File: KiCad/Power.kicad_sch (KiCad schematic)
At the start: 33 parts, among them J11 ATX_POWER_20, J12 Front Panel, Q3 2N3904, SW1 POWER, SW2 RESET, U106 LM7905_TO220, U130 74LS07, U401 74F32, U603 74HCT74, U604 74HCT14, U810 74F08, X1 14.31818MHz, X2 33.333MHz

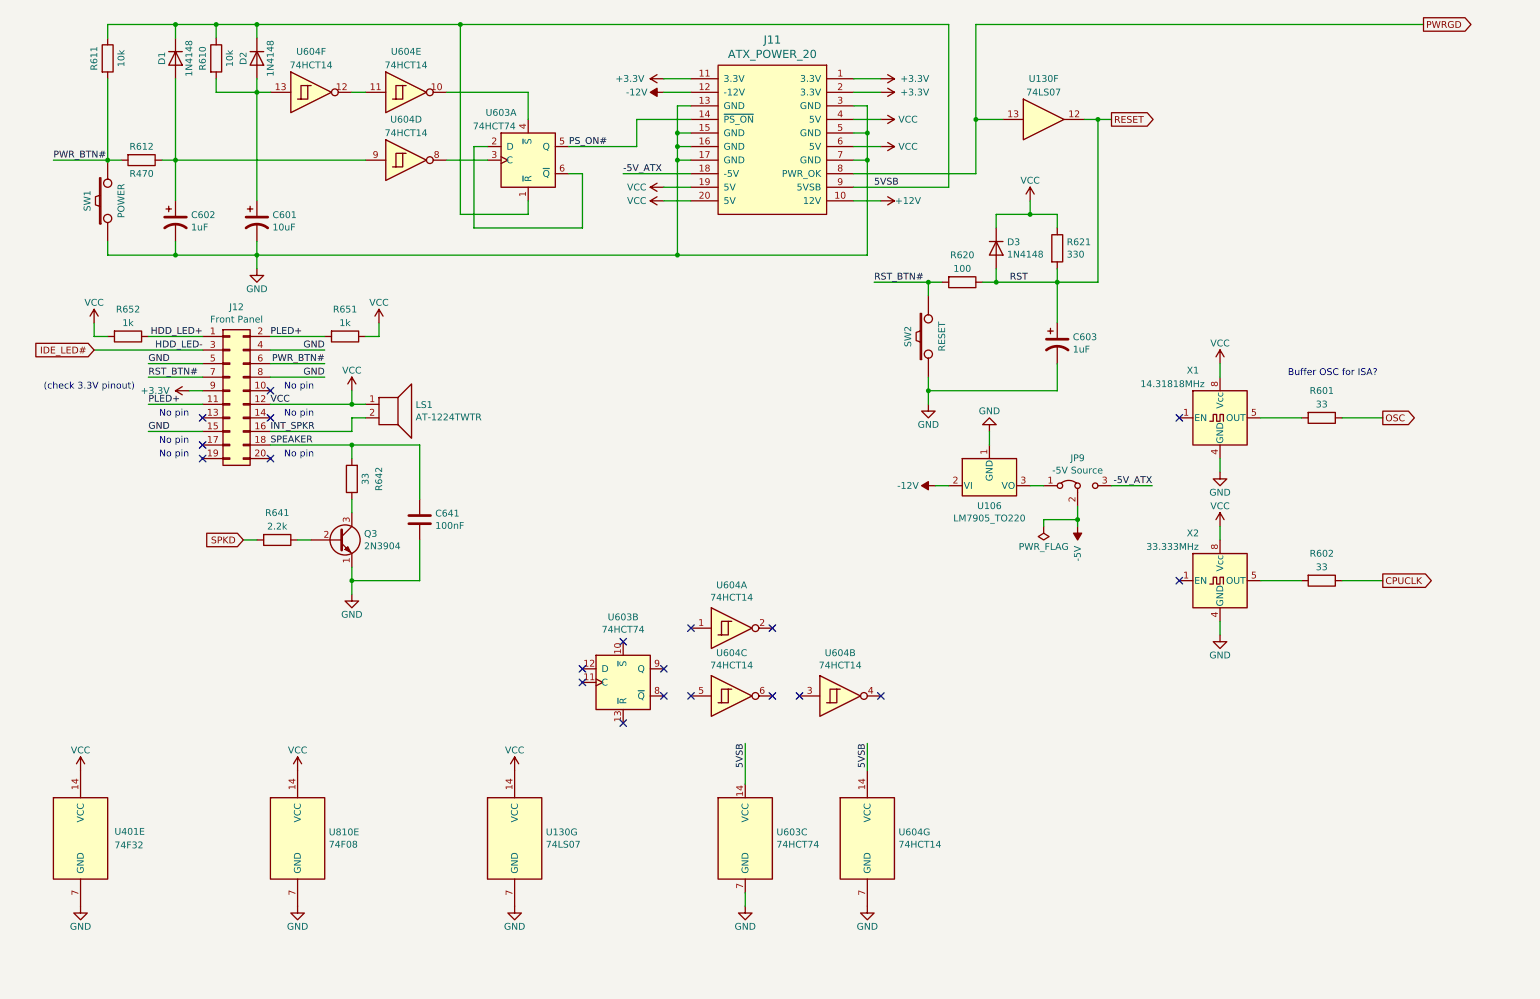
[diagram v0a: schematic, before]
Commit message: Version 0.3: Update DRAM schematic, pull-ups/pull-downs, CPU configuration jumpers
Signed-off-by: Sergey Kiselev <skiselev@gmail.com>
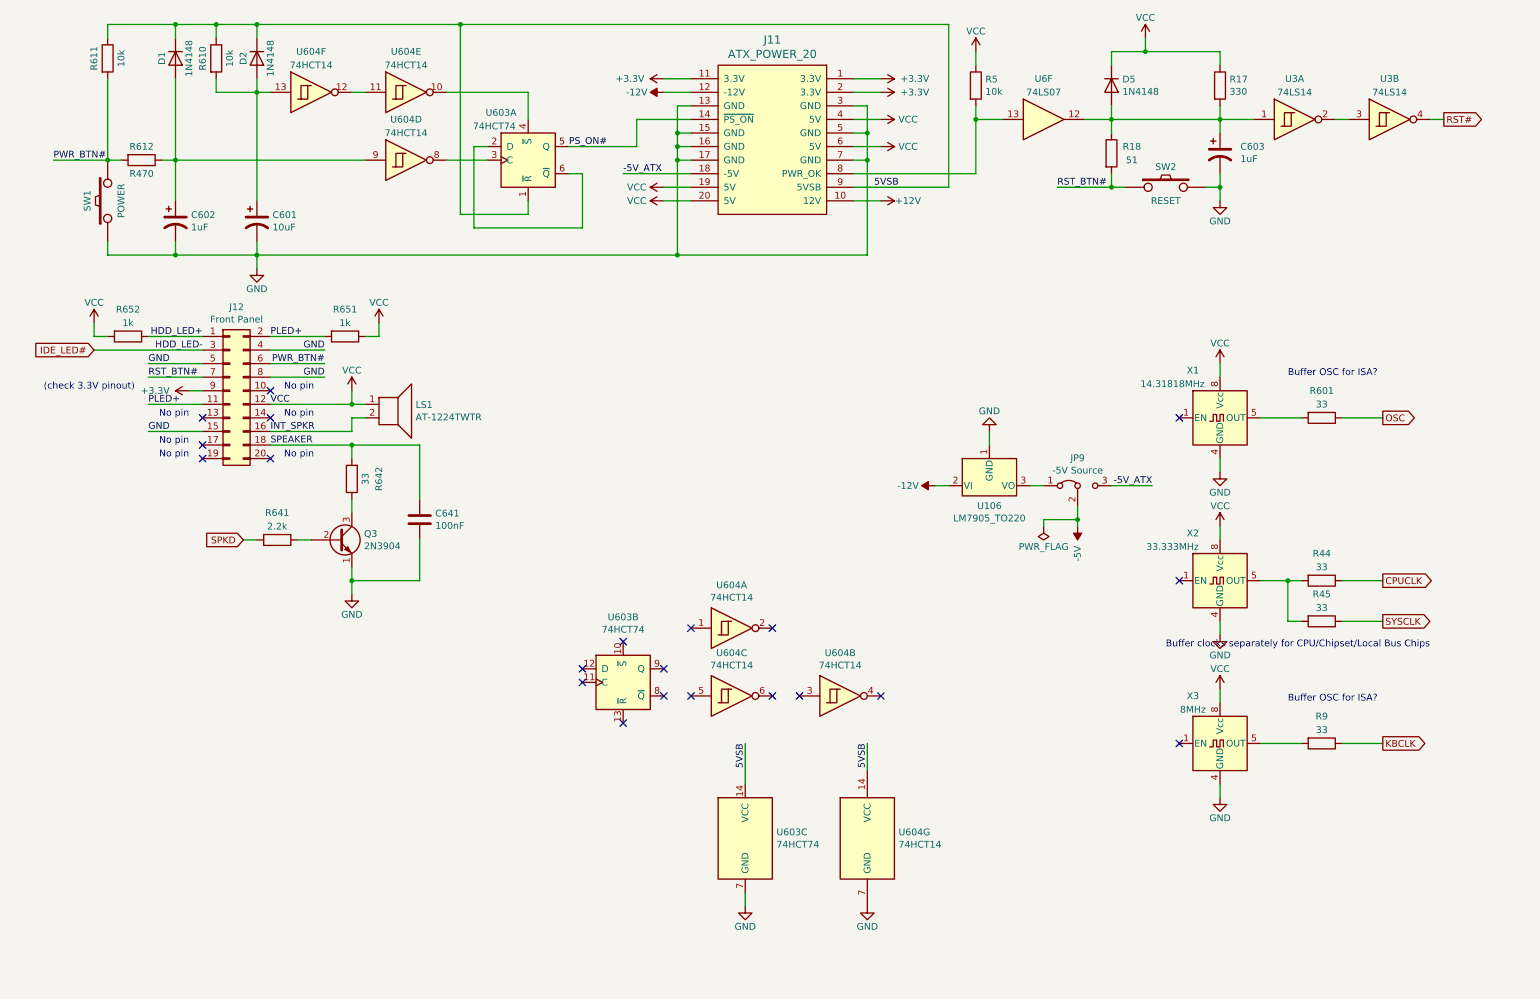
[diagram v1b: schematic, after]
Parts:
- removed U130: 74LS07, symbol 74xx:74LS07
- removed U401: 74F32, symbol 74xx:74LS32
- removed U810: 74F08, symbol 74xx:74LS08
- added R45, R9: 33, symbol Device:R
- added R5: 10k, symbol Device:R
- added U3: 74LS14, symbol 74xx:74LS14
- added U6: 74LS07, symbol 74xx:74LS07
- added X3: 8MHz, Oscillator:Oscillator_DIP-8, symbol Oscillator:CXO_DIP8
- R18: renamed from R620; value 100 -> 51
- renumbered D3 to D5, R621 to R17, R602 to R44
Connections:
- net GND: now also SW2.2, X3.4 (GND); no longer SW2.1
- net RST_BTN#: now also SW2.1; no longer SW2.2
- net VCC: now also R5.1, X3.8 (Vcc)
- net at R44.2, X2.5 (OUT): now also R45.2
- net PWRGD: no longer names the net of J11.8 (PWR_OK)
- net PWRGD: now also R5.2, U6.13
- net RESET: no longer names the net of C603.1, D5.2 (A), R17.2, R18.1
- net RESET: now also U3.1, U6.12
- new net: R9.2, X3.5 (OUT)
- new net: U3.2, U3.3
- new net KBCLK: R9.1
- new net RST#: U3.4
- new net SYSCLK: R45.1
- no-connect marks 20 -> 21
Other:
- note added: "Buffer clocks separately for CPU/Chipset/Local Bus Chips"
- moved on the sheet: C603, D5, R17, R18, SW2

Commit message: Version 0.4: Update chipset connection
Signed-off-by: Sergey Kiselev <skiselev@gmail.com>
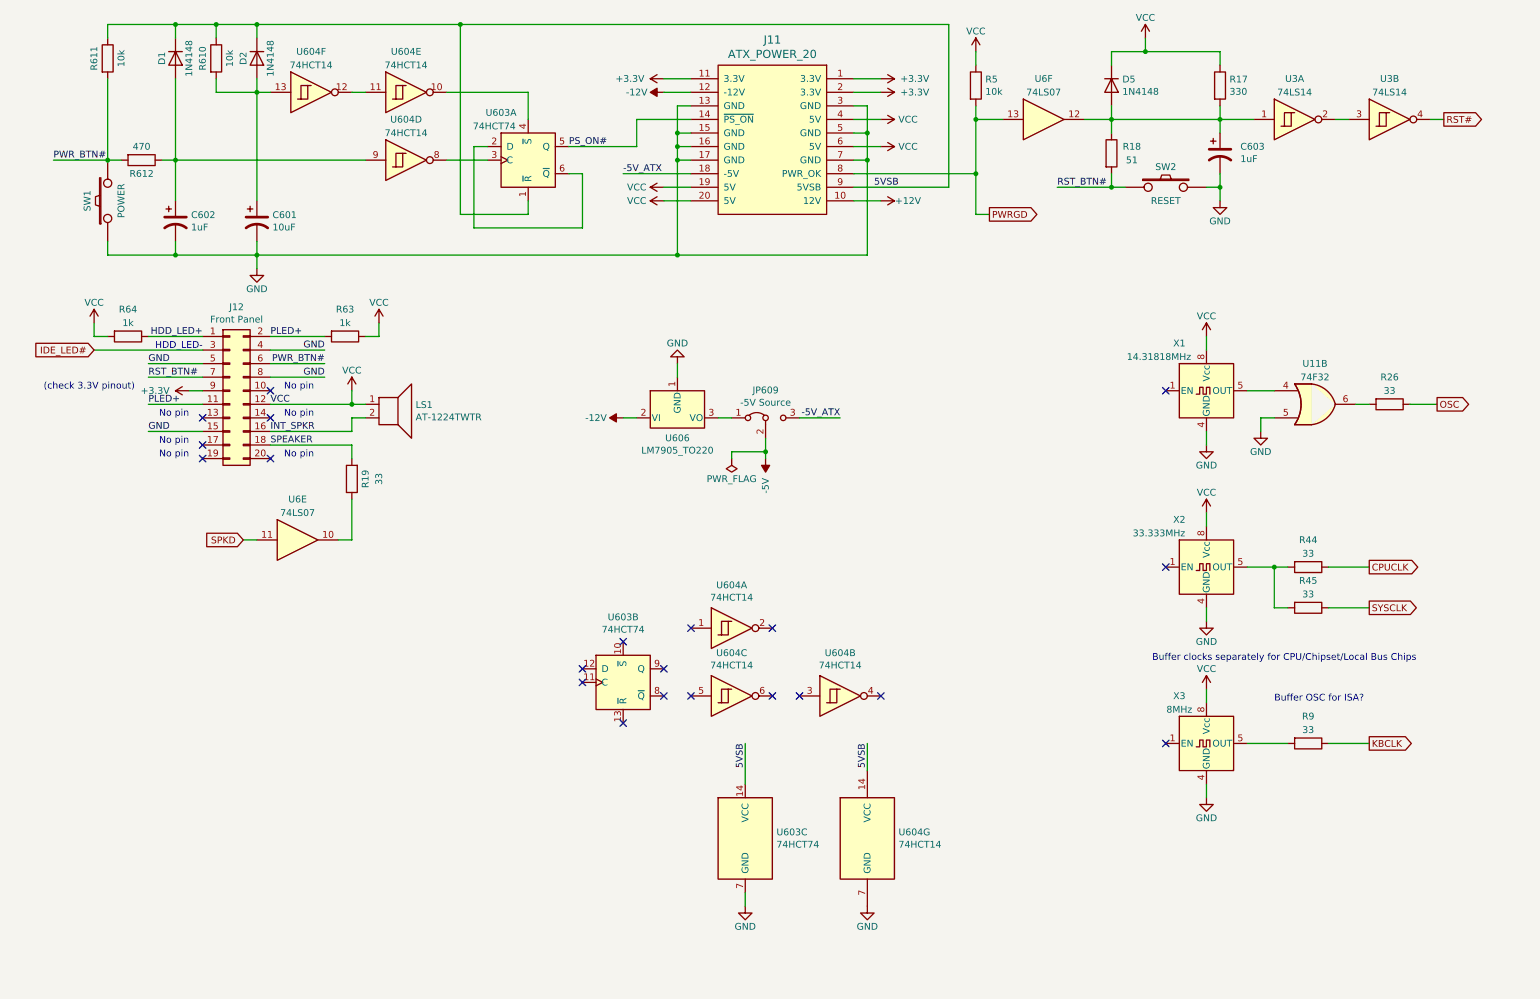
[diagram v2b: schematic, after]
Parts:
- removed C641: 100nF, symbol Device:C
- removed Q3: 2N3904, Package_TO_SOT_THT:TO-92_Inline, symbol Transistor_BJT:2N3904
- removed R641: 2.2k, symbol Device:R
- added U11: 74F32, My_Components:IC_DIP14_300, symbol 74xx:74LS32
- added unit 5 of U6
- C601, C602, C603: footprint (none) -> Capacitor_THT:CP_Radial_D5.0mm_P2.00mm; symbol Device:CP1 -> Device:C_Polarized_US
- D1, D2, D5: footprint (none) -> Diode_THT:D_DO-35_SOD27_P7.62mm_Horizontal
- J11: footprint (none) -> My_Components:Conn_Power_ATX_20pin
- J12: footprint (none) -> Connector_PinHeader_2.54mm:PinHeader_2x10_P2.54mm_Vertical
- JP609: renamed from JP9; footprint (none) -> My_Components:Conn_Pin_Header_3x1_2.54mm
- LS1: footprint (none) -> My_Components:Speaker_12mm
- R17, R18, R44, R45, R5, R610, R611, R9: footprint (none) -> Resistor_SMD:R_0612_1632Metric_Pad1.18x3.40mm_HandSolder
- R19: renamed from R642; footprint (none) -> Resistor_SMD:R_0612_1632Metric_Pad1.18x3.40mm_HandSolder
- R26: renamed from R601; footprint (none) -> Resistor_SMD:R_0612_1632Metric_Pad1.18x3.40mm_HandSolder
- R612: renamed from R470; value R612 -> 470
- R63: renamed from R651; footprint (none) -> Resistor_SMD:R_0612_1632Metric_Pad1.18x3.40mm_HandSolder
- R64: renamed from R652; footprint (none) -> Resistor_SMD:R_0612_1632Metric_Pad1.18x3.40mm_HandSolder
- SW1, SW2: footprint (none) -> My_Components:Switch_Tactile_6mm
- U3, U6, U603, U604: footprint (none) -> My_Components:IC_DIP14_300
- renumbered U106 to U606
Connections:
- net GND: now also U11.5
- net SPKD: now also U6.11
- net at X1.5 (OUT): now also U11.4; no longer R26.2
- net at R19.1: now also U6.10
- net PWRGD: now reaches J11.8 (PWR_OK), R5.2, U6.13
- new net: R26.2, U11.6
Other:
- note added: "HDD_LED-"
- moved on the sheet: JP609, R26, R44, R45, R9, U606, X1, X2, X3

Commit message: More schematic updates. Remove old KiCad files
Signed-off-by: Sergey Kiselev <skiselev@gmail.com>
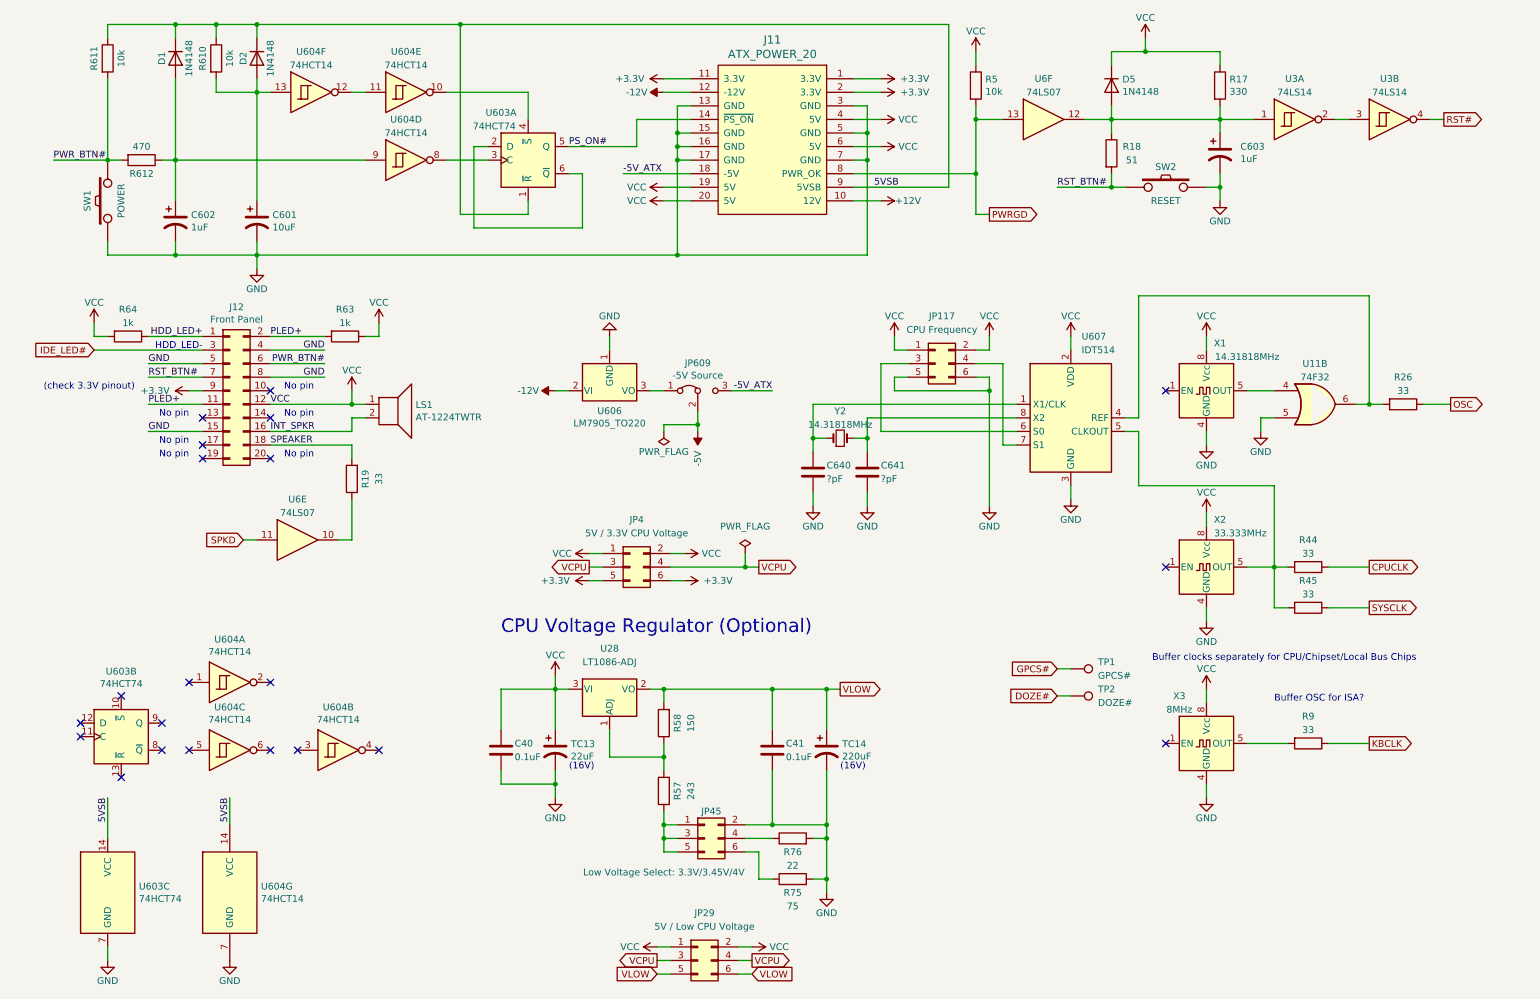
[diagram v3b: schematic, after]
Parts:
- added C40, C41: 0.1uF, symbol Device:C
- added C640, C641: ?pF, Capacitor_SMD:C_0603_1608Metric_Pad1.08x0.95mm_HandSolder, symbol Device:C
- added JP117: CPU Frequency, symbol Connector_Generic:Conn_02x03_Odd_Even
- added JP29: 5V / Low CPU Voltage, symbol Connector_Generic:Conn_02x03_Odd_Even
- added JP4: 5V / 3.3V CPU Voltage, symbol Connector_Generic:Conn_02x03_Odd_Even
- added JP45: Low Voltage Select: 3.3V/3.45V/4V, symbol Connector_Generic:Conn_02x03_Odd_Even
- added R57: 243, symbol Device:R
- added R58: 150, symbol Device:R
- added R75: 75, symbol Device:R
- added R76: 22, symbol Device:R
- added TC13: 22uF, Capacitor_THT:CP_Radial_D5.0mm_P2.00mm, symbol Device:C_Polarized_US
- added TC14: 220uF, Capacitor_THT:CP_Radial_D5.0mm_P2.00mm, symbol Device:C_Polarized_US
- added TP1: GPCS#, symbol Connector:TestPoint
- added TP2: DOZE#, symbol Connector:TestPoint
- added U28: LT1086-ADJ, symbol Regulator_Linear:LT1086-ADJ
- added U607: IDT514, Package_SO:SOIC-8_3.9x4.9mm_P1.27mm, symbol Oscillator:NB3N502
- added Y2: 14.31818MHz, My_Components:Crystal_32K_Horiz, symbol Device:Crystal_Small
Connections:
- net +3V3: now also JP4.5 (Pin_5), JP4.6 (Pin_6)
- net GND: now also C40.2, C41.2, C640.2, C641.2, JP117.5 (Pin_5), JP117.6 (Pin_6), JP45.2 (Pin_2), R75.2, R76.2, TC13.2, TC14.2, U607.3 (GND)
- net VCC: now also C40.1, JP117.1 (Pin_1), JP117.2 (Pin_2), JP29.1 (Pin_1), JP29.2 (Pin_2), JP4.1 (Pin_1), JP4.2 (Pin_2), TC13.1, U28.3 (VI), U607.2 (VDD)
- net at R26.2, U11.6: now also U607.4 (REF)
- net at R44.2, R45.2, X2.5 (OUT): now also U607.5 (CLKOUT)
- new net: C640.1, U607.1 (X1/CLK), Y2.1
- new net: JP45.1 (Pin_1), JP45.3 (Pin_3), JP45.5 (Pin_5), R57.1
- new net: R57.2, R58.1, U28.1 (ADJ)
- new net: C641.1, U607.8 (X2), Y2.2
- new net: JP45.4 (Pin_4), R76.1
- new net: JP45.6 (Pin_6), R75.1
- new net: JP117.3 (Pin_3), U607.6 (S0)
- new net: JP117.4 (Pin_4), U607.7 (S1)
- new net DOZE#: TP2.1
- new net GPCS#: TP1.1
- new net VCPU: JP29.3 (Pin_3), JP29.4 (Pin_4), JP4.3 (Pin_3), JP4.4 (Pin_4)
- new net VLOW: C41.1, JP29.5 (Pin_5), JP29.6 (Pin_6), R58.2, TC14.1, U28.2 (VO)
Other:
- note added: "(16V)"
- note added: "CPU Voltage Regulator (Optional)"
- moved on the sheet: JP609, R26, U603B, U603C, U604A, U604B, U604C, U604G, U606
